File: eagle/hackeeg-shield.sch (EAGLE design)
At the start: 140 parts, among them IC1 ADS1299IPAG, IC2 TPS72325DBVT, IC3 TPS73225DBVT, IC5 24AA256UID, IC6 TPS60403DBVT, IC7 OPA376DBV, IC8 OPA376DBV, IC9 TXS0102DCUR, J16 EXTERNAL_SYNC, J8 Electrode Connector, U2 TXB0108PWR, U3 TXB0108PWR

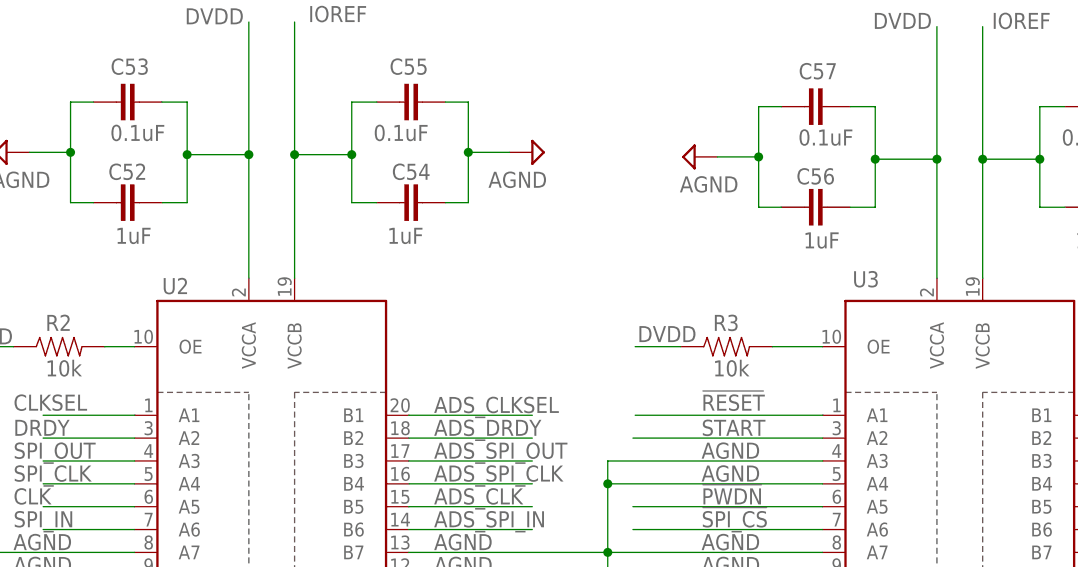
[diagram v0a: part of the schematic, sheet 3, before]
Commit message: updates to fix keepout errors; minor silkscreen improvements
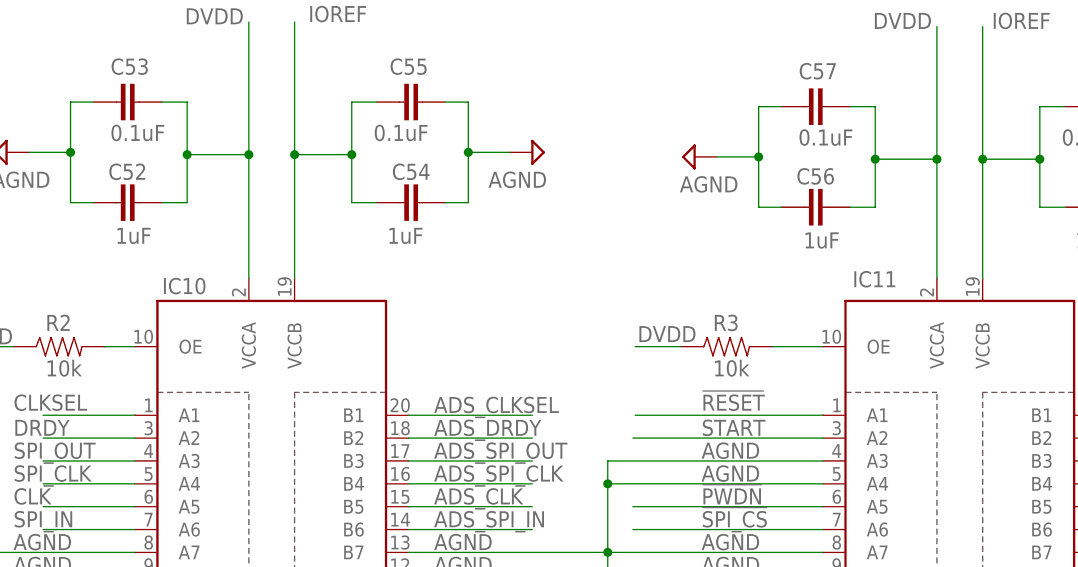
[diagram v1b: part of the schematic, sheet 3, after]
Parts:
- renumbered U2 to IC10, U3 to IC11

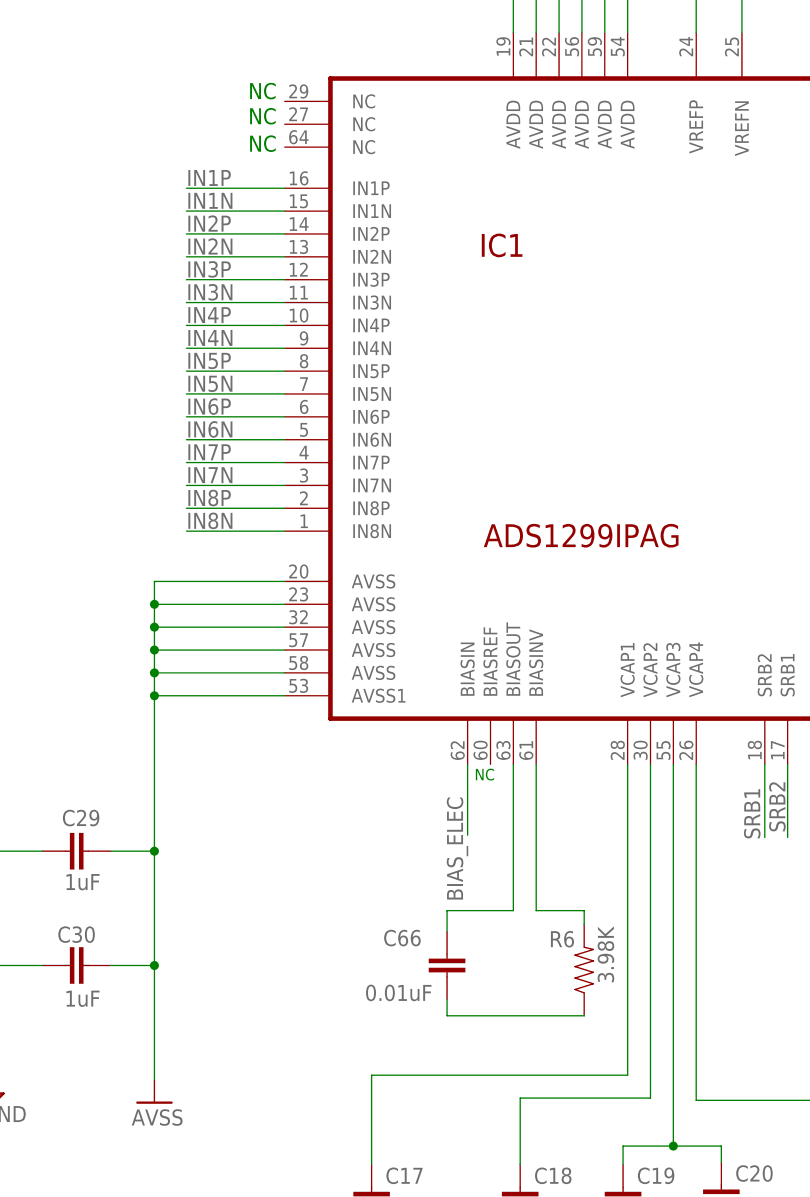
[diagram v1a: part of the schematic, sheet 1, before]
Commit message: fixed Analog Input filter bug; added BIASINV signal to electrode connector and to unused power connector pin, with solder jumper; improved trace clearances
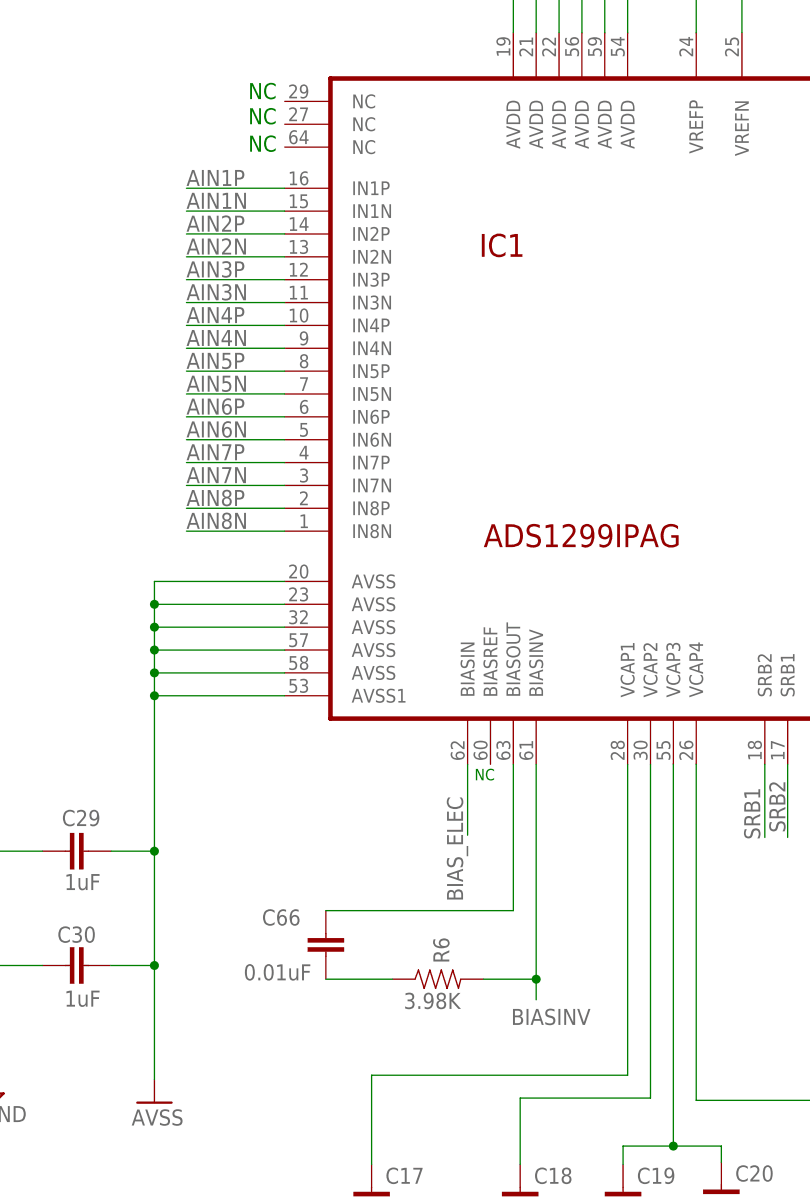
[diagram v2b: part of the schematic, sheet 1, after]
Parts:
- added SJ1: SOLDERJUMPERNO, SparkFun-Passives:SOLDERJUMPERNO
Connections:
- removed net N$12: IC1.BIASINV, R6.2
- new net BIASINV: IC1.BIASINV, J8.3, J8.4, R6.2, SJ1.1
- net AGND: no longer J8.3, J8.4
- net AIN1N: now also IC1.IN1N; no longer J8.8
- net AIN1P: now also IC1.IN1P; no longer J8.7
- net AIN2N: now also IC1.IN2N; no longer J8.10
- net AIN2P: now also IC1.IN2P; no longer J8.9
- net AIN3N: now also IC1.IN3N; no longer J8.12
- net AIN3P: now also IC1.IN3P; no longer J8.11
- net AIN4N: now also IC1.IN4N; no longer J8.14
- net AIN4P: now also IC1.IN4P; no longer J8.13
- net AIN5N: now also IC1.IN5N; no longer J8.16
- net AIN5P: now also IC1.IN5P; no longer J8.15
- net AIN6N: now also IC1.IN6N; no longer J8.18
- net AIN6P: now also IC1.IN6P; no longer J8.17
- net AIN7N: now also IC1.IN7N; no longer J8.20
- net AIN7P: now also IC1.IN7P; no longer J8.19
- net AIN8N: now also IC1.IN8N; no longer J8.22
- net AIN8P: now also IC1.IN8P; no longer J8.21
- net IN1N: now also J8.8; no longer IC1.IN1N
- net IN1P: now also J8.7; no longer IC1.IN1P
- net IN2N: now also J8.10; no longer IC1.IN2N
- net IN2P: now also J8.9; no longer IC1.IN2P
- net IN3N: now also J8.12; no longer IC1.IN3N
- net IN3P: now also J8.11; no longer IC1.IN3P
- net IN4N: now also J8.14; no longer IC1.IN4N
- net IN4P: now also J8.13; no longer IC1.IN4P
- net IN5N: now also J8.16; no longer IC1.IN5N
- net IN5P: now also J8.15; no longer IC1.IN5P
- net IN6N: now also J8.18; no longer IC1.IN6N
- net IN6P: now also J8.17; no longer IC1.IN6P
- net IN7N: now also J8.20; no longer IC1.IN7N
- net IN7P: now also J8.19; no longer IC1.IN7P
- net IN8N: now also J8.22; no longer IC1.IN8N
- net IN8P: now also J8.21; no longer IC1.IN8P
- net N$21: now also SJ1.2
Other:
- moved on the sheet: C66, R6

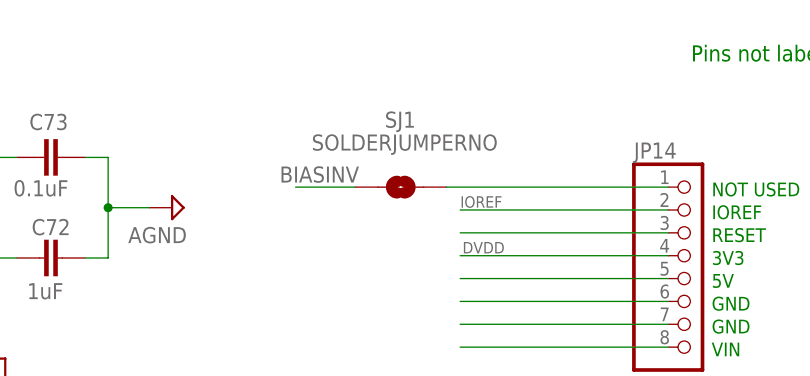
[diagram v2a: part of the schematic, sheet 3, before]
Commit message: minor changes to BIASINV solder pad
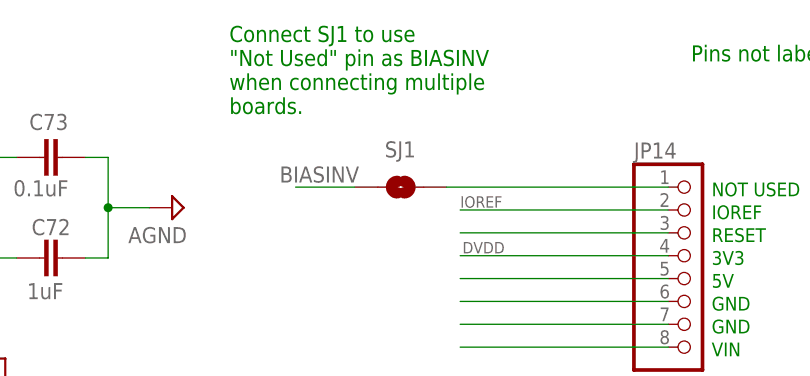
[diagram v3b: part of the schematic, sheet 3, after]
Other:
- note added: "Connect SJ1 to use "Not Used" pin as BIASINV when connecting multiple boards."
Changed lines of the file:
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@@
 <text x="358.902" y="233.172" size="1.524" layer="91">D9</text>
 <text x="359.156" y="230.886" size="1.524" layer="91">D8</text>
+<text x="253.492" y="258.318" size="1.778" layer="91">Connect SJ1 to use
+"Not Used" pin as BIASINV
+when connecting multiple
+boards.</text>
 </plain>
 <instances>
@@
 </instance>
 <instance part="SJ1" gate="1" x="272.542" y="250.19" smashed="yes">
-<attribute name="NAME" x="270.764" y="256.794" size="1.778" layer="95"/>
-<attribute name="VALUE" x="262.636" y="254.254" size="1.778" layer="96"/>
+<attribute name="NAME" x="270.764" y="253.492" size="1.778" layer="95"/>
 </instance>
 </instances>

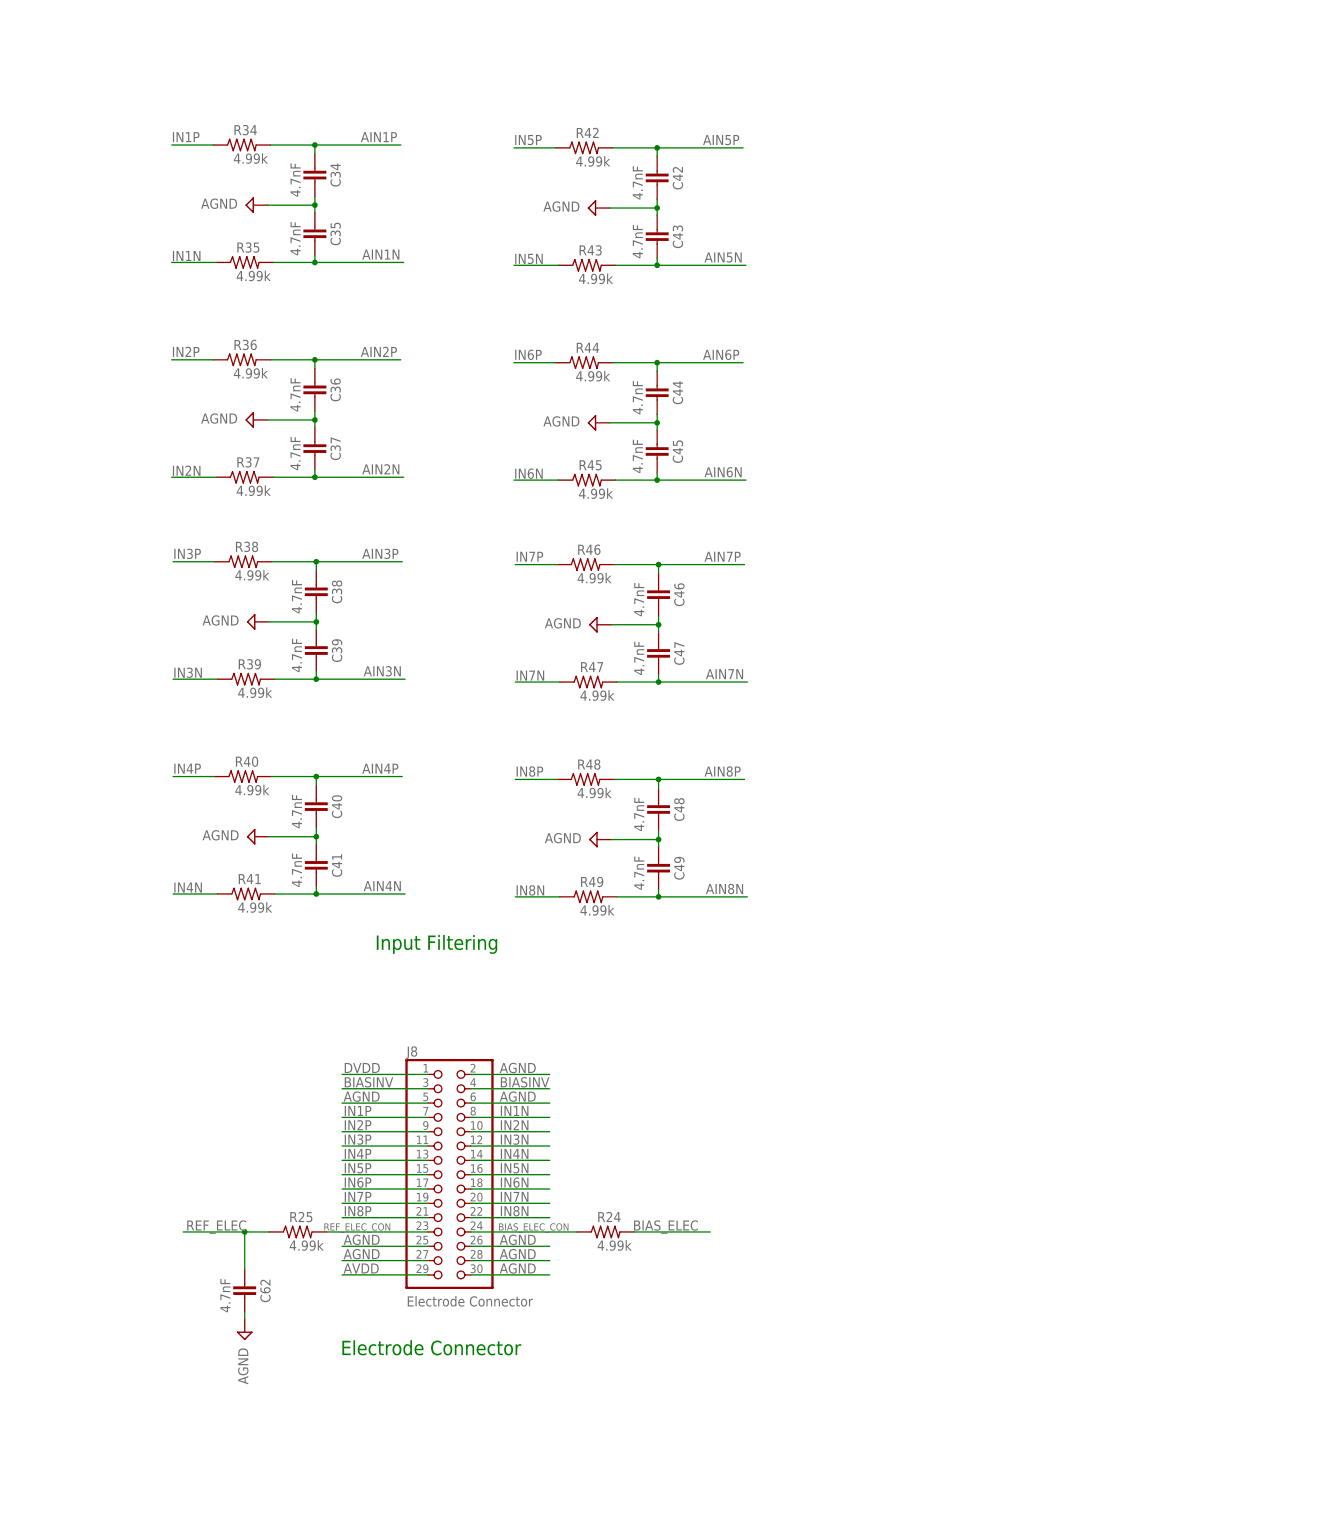
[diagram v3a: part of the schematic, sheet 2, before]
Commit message: switched to 24 position electrode connector (from 30); changed sync connector to 4-position (from 3 position); added BIASINV signal to sync connector; changed electrode connector and analog filtering schematic layout to be more readable
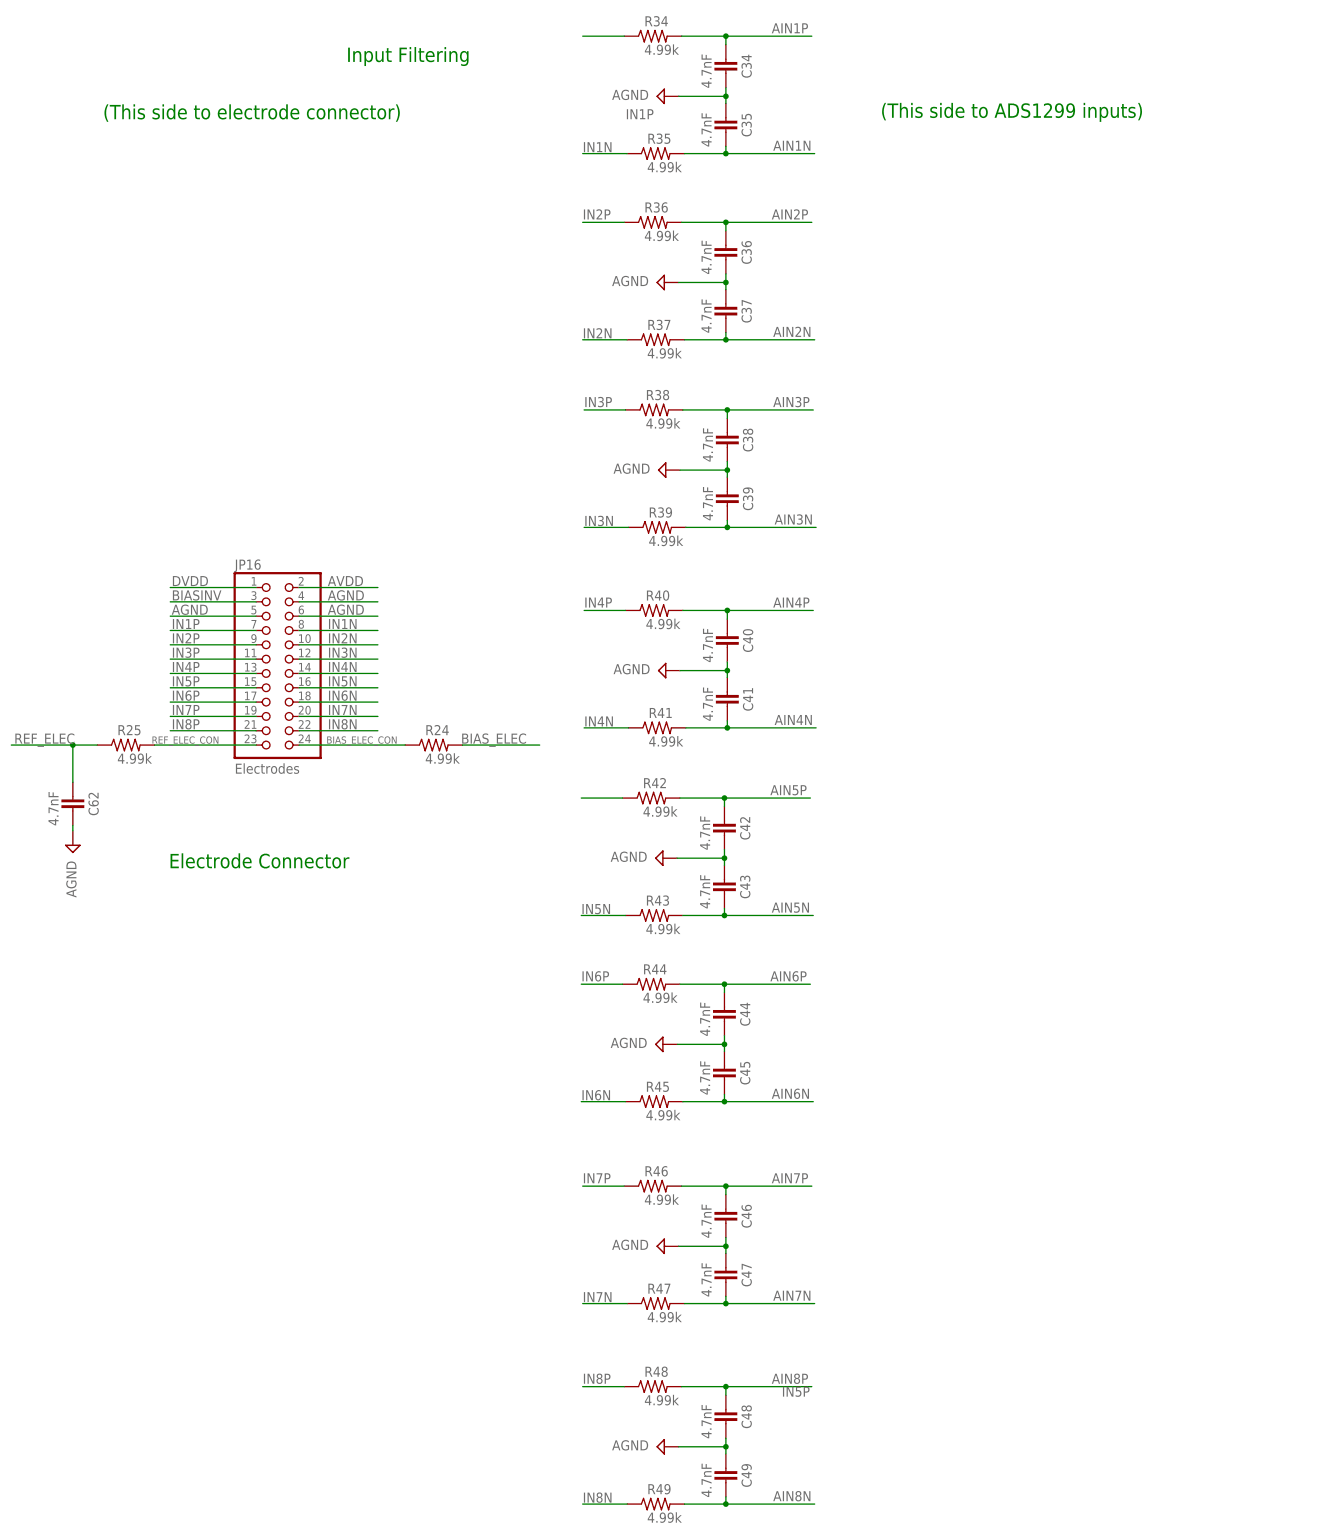
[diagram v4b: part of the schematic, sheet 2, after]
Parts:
- removed J16: EXTERNAL_SYNC, SparkFun-Connectors:M03JST-PTH
- removed J8: Electrode Connector, headers:PINHD-2X15
- removed SJ1: SOLDERJUMPERNO, SparkFun-Passives:SOLDERJUMPERNO
- added JP15: External Sync, SparkFun-Connectors:M04JST-PTH
- added JP16: Electrodes, headers:PINHD-2X12
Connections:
- net ADS_SPI_CLK: now also JP15.3; no longer J16.1
- net ADS_START: now also JP15.2; no longer J16.3
- net AGND: now also JP15.4, JP16.4, JP16.5, JP16.6; no longer J16.2, J8.2, J8.25, J8.26, J8.27, J8.28, J8.30, J8.5, J8.6
- net AVDD: now also JP16.2; no longer J8.29
- net BIASINV: now also JP15.1, JP16.3; no longer J8.3, J8.4, SJ1.1
- net BIAS_ELEC_CON: now also JP16.24; no longer J8.24
- net DVDD: now also JP16.1; no longer J8.1
- net IN1N: now also JP16.8; no longer J8.8
- net IN1P: now also JP16.7; no longer J8.7
- net IN2N: now also JP16.10; no longer J8.10
- net IN2P: now also JP16.9; no longer J8.9
- net IN3N: now also JP16.12; no longer J8.12
- net IN3P: now also JP16.11; no longer J8.11
- net IN4N: now also JP16.14; no longer J8.14
- net IN4P: now also JP16.13; no longer J8.13
- net IN5N: now also JP16.16; no longer J8.16
- net IN5P: now also JP16.15; no longer J8.15
- net IN6N: now also JP16.18; no longer J8.18
- net IN6P: now also JP16.17; no longer J8.17
- net IN7N: now also JP16.20; no longer J8.20
- net IN7P: now also JP16.19; no longer J8.19
- net IN8N: now also JP16.22; no longer J8.22
- net IN8P: now also JP16.21; no longer J8.21
- net N$21: no longer SJ1.2
- net REF_ELEC_CON: now also JP16.23; no longer J8.23
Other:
- note added: "(This side to ADS1299 inputs)"
- note added: "(This side to electrode connector)"
- note removed: "Connect SJ1 to use "Not Used" pin as BIASINV when connecting multiple boards."
- note removed: "External sync connector"
- moved on the sheet: C34, C35, C36, C37, C38, C39, C40, C41, C42, C43, C44, C45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
